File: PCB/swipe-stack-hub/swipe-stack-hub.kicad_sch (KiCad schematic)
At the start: 10 parts, among them J1 Barrel_Jack_Switch, U1 STM32F091RCTx, U2 LMR51430 (LMR54410), U3 CC2640R2FRGZR

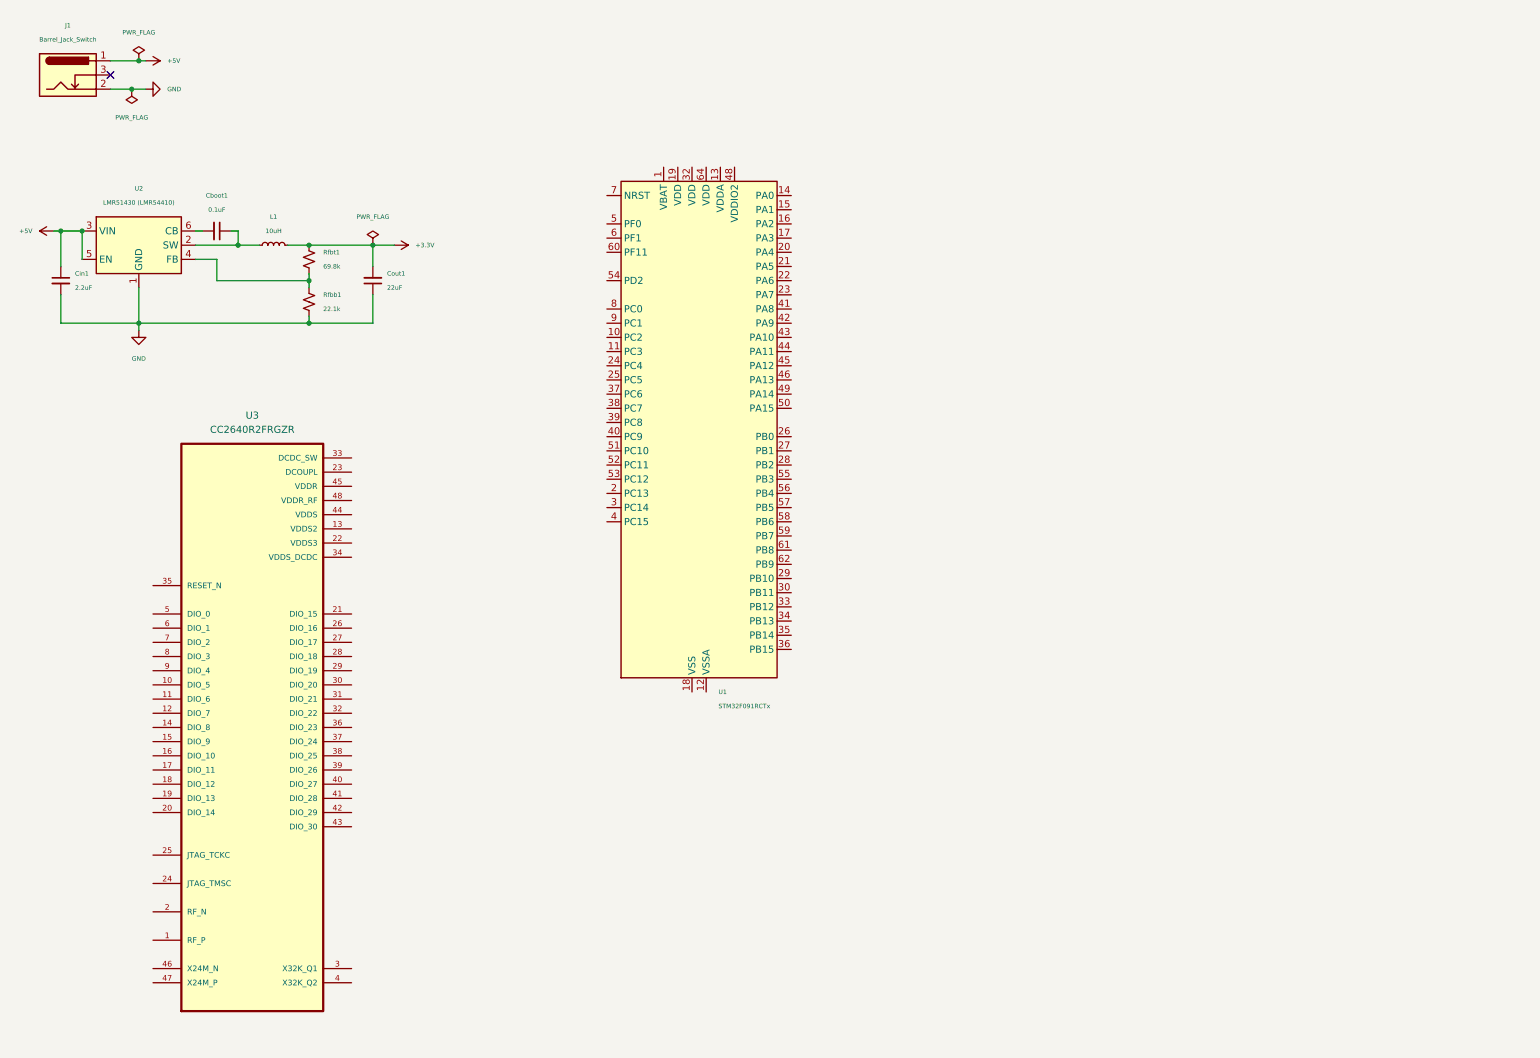
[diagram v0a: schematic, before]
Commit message: Updated swipe-stack hub schematic with HM19 modules as well as reset button circuitry for MCU
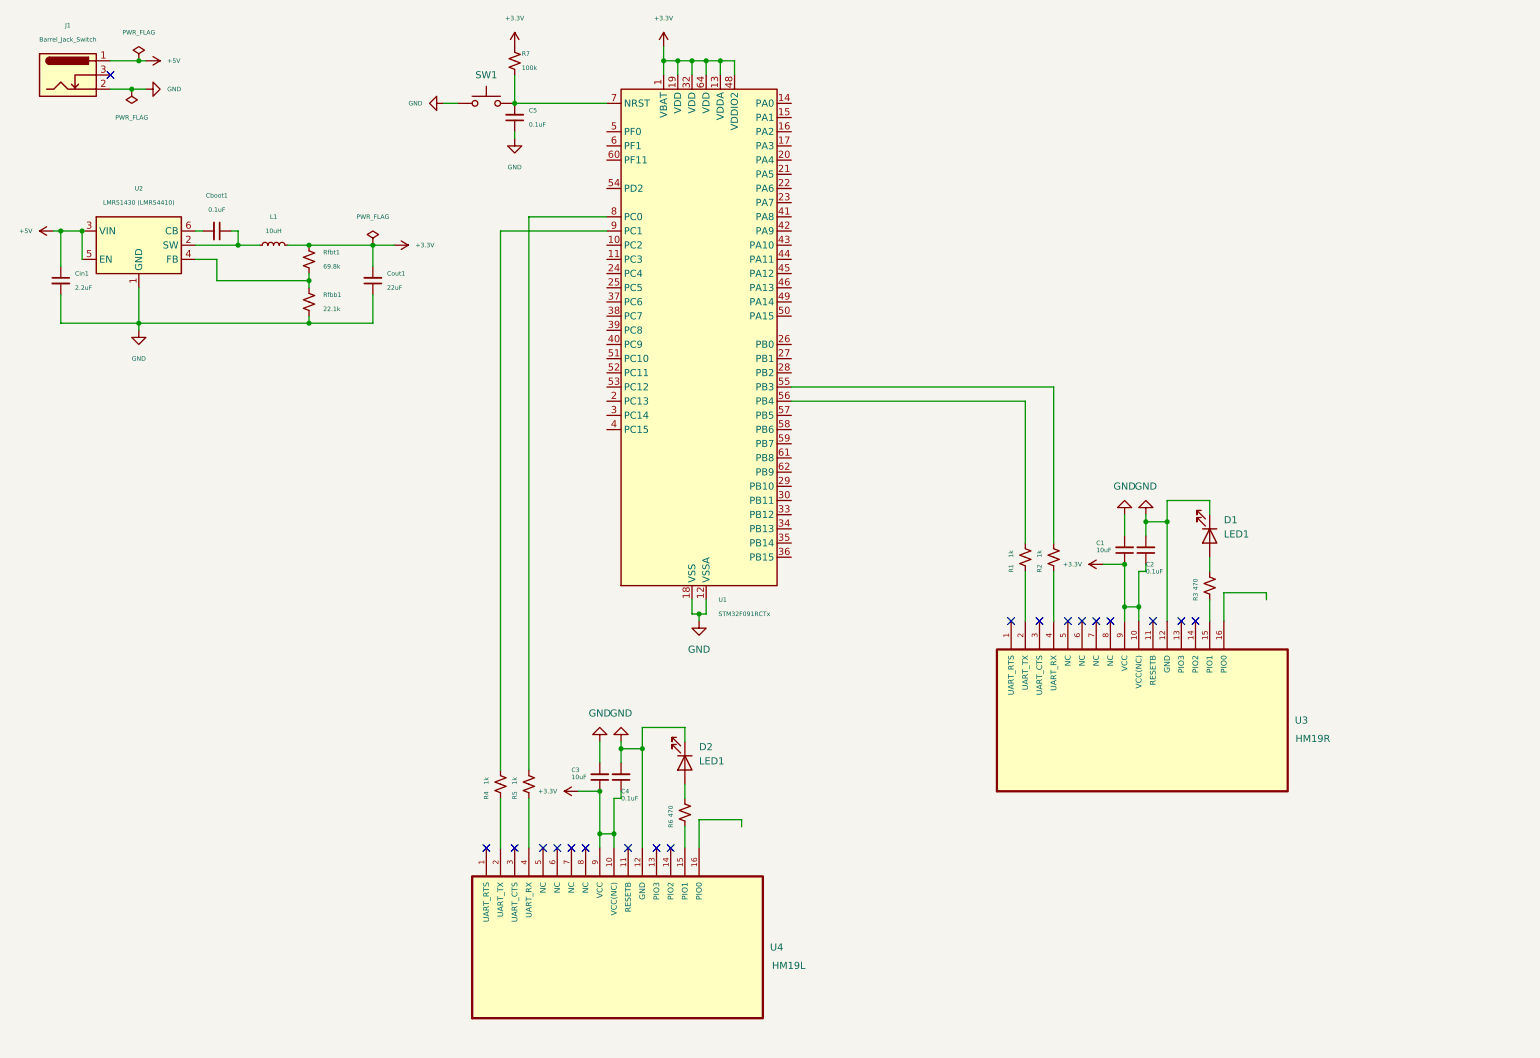
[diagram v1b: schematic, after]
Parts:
- removed U3: CC2640R2FRGZR, cc:QFN50P700X700X100-49N, symbol CC2640R2FRGZR:CC2640R2FRGZR
- added C1, C3: 10uF, symbol Device:C_Small
- added C2, C4, C5: 0.1uF, symbol Device:C_Small
- added D1, D2: LED1, symbol Device:LED
- added R1, R2, R4, R5: 1k, symbol Device:R_Small_US
- added R3, R6: 470, symbol Device:R_Small_US
- added R7: 100k, symbol Device:R_Small_US
- added SW1: ~, symbol Switch:SW_Push
- added U3: HM19R, hm:HM-11-MODULE, symbol HM11-19:CC2640R2FRGZR
- added U4: HM19L, hm:HM-11-MODULE, symbol HM11-19:CC2640R2FRGZR
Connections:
- net +3.3V: now also U1.1 (VBAT), U1.13 (VDDA), U1.19 (VDD), U1.32 (VDD), U1.48 (VDDIO2), U1.64 (VDD), C1.1, C2.1, C3.1, C4.1, R7.1, U3.10 (VCC(NC)), U3.9 (VCC), U4.10 (VCC(NC)), U4.9 (VCC)
- net GND: now also U1.12 (VSSA), U1.18 (VSS), U1.31 (VSS), U1.47 (VSS), U1.63 (VSS), C1.2, C2.2, C3.2, C4.2, C5.1, D1.1 (K), D2.1 (K), SW1.1, U3.12 (GND), U4.12 (GND)
- net at U1.55 (PB3): now also R2.2
- net at U1.56 (PB4): now also R1.2
- net at U1.7 (NRST): now also C5.2, R7.2, SW1.2
- net at U1.8 (PC0): now also R5.2
- net at U1.9 (PC1): now also R4.2
- new net: R3.1, U3.15 (PIO1)
- new net: D1.2 (A), R3.2
- new net: R1.1, U3.2 (UART_TX)
- new net: R4.1, U4.2 (UART_TX)
- new net: R5.1, U4.4 (UART_RX)
- new net: R6.1, U4.15 (PIO1)
- new net: D2.2 (A), R6.2
- new net: R2.1, U3.4 (UART_RX)
- no-connect marks 1 -> 19
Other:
- moved on the sheet: U1

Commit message: First cut of hub PCB
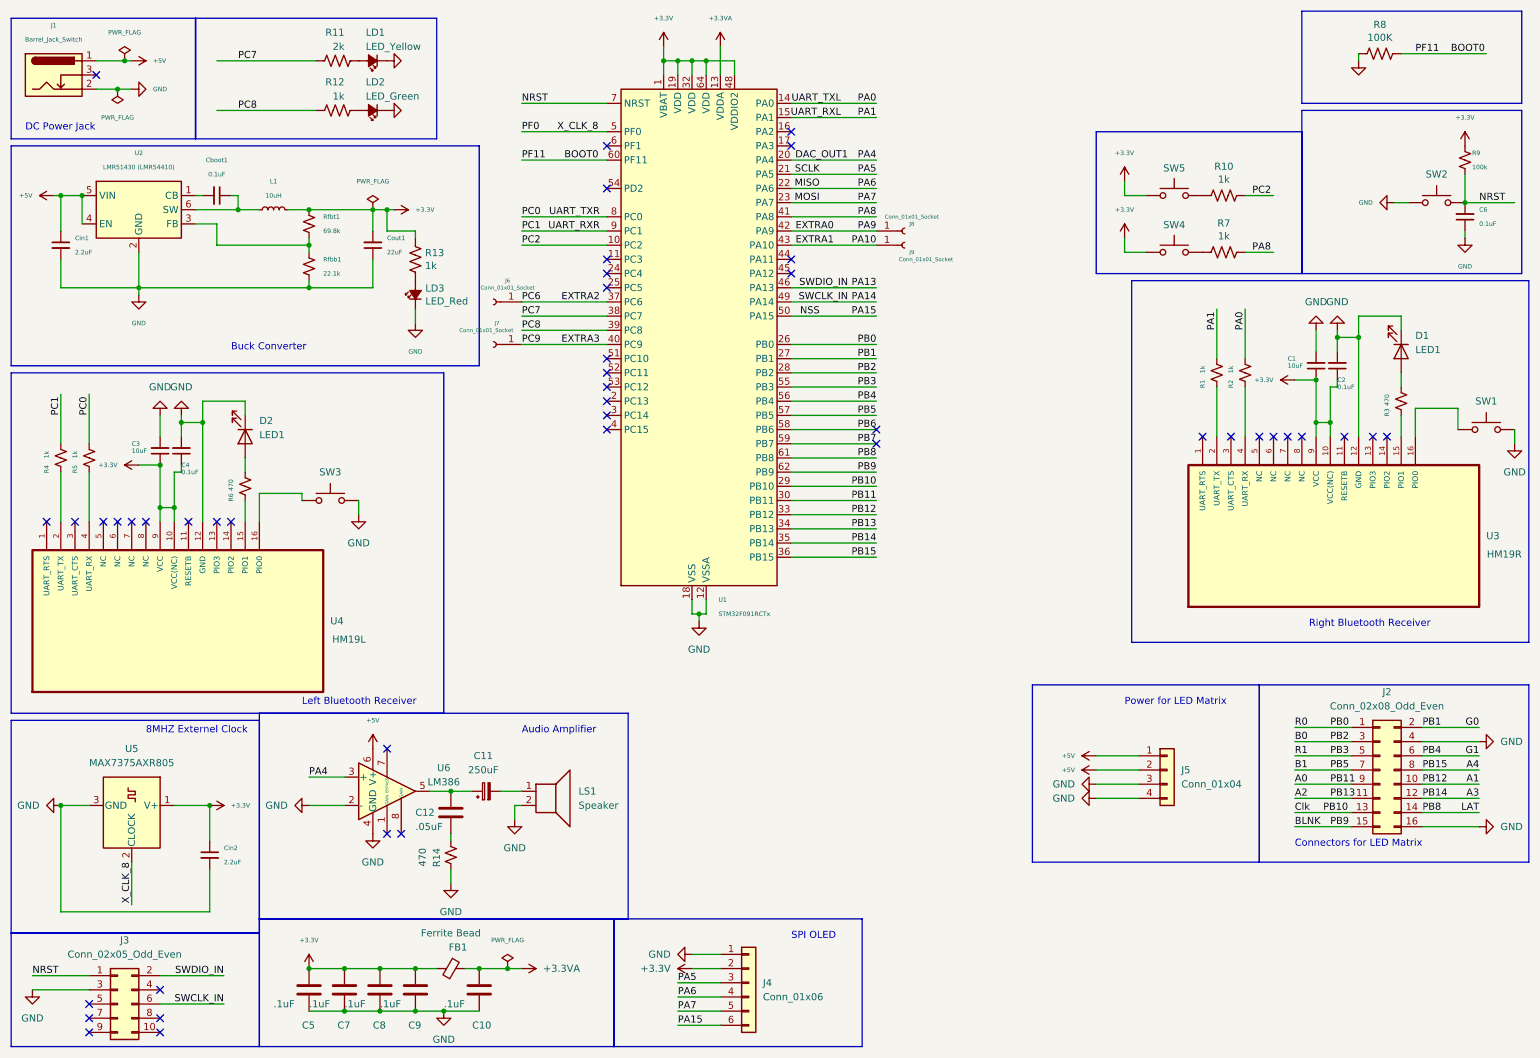
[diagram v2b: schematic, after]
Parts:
- removed C5: 0.1uF, symbol Device:C_Small
- removed R7: 100k, symbol Device:R_Small_US
- added C10, C5, C7, C8, C9: .1uF, Capacitor_SMD:C_0805_2012Metric_Pad1.18x1.45mm_HandSolder, symbol Device:C
- added C11: 250uF, Capacitor_SMD:C_0805_2012Metric_Pad1.18x1.45mm_HandSolder, symbol Device:C_Polarized_Small
- added C12: .05uF, Capacitor_SMD:C_0805_2012Metric_Pad1.18x1.45mm_HandSolder, symbol Device:C
- added C6: 0.1uF, Capacitor_SMD:C_0805_2012Metric_Pad1.18x1.45mm_HandSolder, symbol Device:C_Small
- added Cin2: 2.2uF, Capacitor_SMD:C_0805_2012Metric_Pad1.18x1.45mm_HandSolder, symbol Device:C_Small
- added FB1: Ferrite Bead, Inductor_SMD:L_0805_2012Metric_Pad1.15x1.40mm_HandSolder, symbol stm32f091-rescue:Ferrite_Bead_Small-Device
- added J2: Conn_02x08_Odd_Even, Connector_IDC:IDC-Header_2x08_P2.54mm_Vertical_SMD, symbol Connector_Generic:Conn_02x08_Odd_Even
- added J3: Conn_02x05_Odd_Even, Connector_IDC:IDC-Header_2x05_P2.54mm_Vertical_SMD, symbol Connector_Generic:Conn_02x05_Odd_Even
- added J4: Conn_01x06, Connector_JST:JST_EH_B6B-EH-A_1x06_P2.50mm_Vertical, symbol Connector_Generic:Conn_01x06
- added J5: Conn_01x04, Connector_JST:JST_EH_B4B-EH-A_1x04_P2.50mm_Vertical, symbol Connector_Generic:Conn_01x04
- added J6, J7, J8, J9: Conn_01x01_Socket, Connector_PinSocket_2.54mm:PinSocket_1x01_P2.54mm_Vertical, symbol Connector:Conn_01x01_Socket
- added LD1: LED_Yellow, LED_SMD:LED_0805_2012Metric_Pad1.15x1.40mm_HandSolder, symbol stm32f091-rescue:LED_Small_ALT-Device
- added LD2: LED_Green, LED_SMD:LED_0805_2012Metric_Pad1.15x1.40mm_HandSolder, symbol stm32f091-rescue:LED_Small_ALT-Device
- added LD3: LED_Red, LED_SMD:LED_0805_2012Metric_Pad1.15x1.40mm_HandSolder, symbol stm32f091-rescue:LED_Small_ALT-Device
- added LS1: Speaker, symbol Device:Speaker
- added R10, R12, R13, R7: 1k, Resistor_SMD:R_0805_2012Metric_Pad1.20x1.40mm_HandSolder, symbol Device:R_US
- added R11: 2k, Resistor_SMD:R_0805_2012Metric_Pad1.20x1.40mm_HandSolder, symbol Device:R_US
- added R14: 470, Resistor_SMD:R_0805_2012Metric_Pad1.20x1.40mm_HandSolder, symbol Device:R_Small_US
- added R8: 100K, Resistor_SMD:R_0805_2012Metric_Pad1.20x1.40mm_HandSolder, symbol Device:R_US
- added R9: 100k, Resistor_SMD:R_0805_2012Metric_Pad1.20x1.40mm_HandSolder, symbol Device:R_Small_US
- added SW2, SW3: ~, Button_Switch_SMD:SW_SPST_PTS645, symbol Switch:SW_Push
- added SW4, SW5: SW_Push, Button_Switch_SMD:SW_SPST_PTS645, symbol Switch:SW_Push
- added U5: MAX7375AXR805, Package_TO_SOT_SMD:SOT-323_SC-70_Handsoldering, symbol Oscillator:MAX7375AXR805
- added U6: LM386, Package_SO:SOIC-8-1EP_3.9x4.9mm_P1.27mm_EP2.29x3mm, symbol Amplifier_Audio:LM386
- C1, C2, C3, C4, Cboot1, Cin1, Cout1: footprint (none) -> Capacitor_SMD:C_0805_2012Metric_Pad1.18x1.45mm_HandSolder
- D1, D2: footprint (none) -> LED_SMD:LED_0805_2012Metric_Pad1.15x1.40mm_HandSolder
- L1: footprint (none) -> Inductor_SMD:L_0805_2012Metric_Pad1.15x1.40mm_HandSolder
- R1, R2, R3, R4, R5, R6, Rfbb1, Rfbt1: footprint (none) -> Resistor_SMD:R_0805_2012Metric_Pad1.20x1.40mm_HandSolder
- SW1: footprint (none) -> Button_Switch_SMD:SW_SPST_PTS645
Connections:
- net +3.3V: now also C5.1, C7.1, C8.1, C9.1, Cin2.1, FB1.2, J4.2 (Pin_2), R13.1, R9.1, SW4.1, SW5.1, U5.1 (V+); no longer U1.13 (VDDA)
- net +5V: now also U2.4 (EN), J5.1 (Pin_1), J5.2 (Pin_2), U6.6 (V+); no longer U2.3 (VIN)
- net GND: now also SW1.2, U2.2 (GND), C10.2, C5.2, C6.1, C7.2, C8.2, C9.2, Cin2.2, J2.16 (Pin_16), J2.4 (Pin_4), J3.3 (Pin_3), J4.1 (Pin_1), J5.3 (Pin_3), J5.4 (Pin_4), LD1.1 (K), LD2.1 (K), LD3.1 (K), LS1.2, R14.1, R8.2, SW2.1, SW3.2, U5.3 (GND), U6.2 (-), U6.4 (GND); no longer SW1.1, U2.1 (GND)
- net at Rfbb1.1, Rfbt1.2: now also U2.3 (FB); no longer U2.4 (FB)
- net G1: now reaches U1.56 (PB4)
- net G1: now also J2.6 (Pin_6); no longer R1.2
- net at Cboot1.1, L1.1: now also U2.6 (SW); no longer U2.2 (SW)
- net PC1: now reaches R4.2, U1.9 (PC1)
- net NRST: now reaches U1.7 (NRST)
- net NRST: now also C6.2, J3.1 (Pin_1), R9.2, SW2.2; no longer SW1.2
- net PC0: now reaches R5.2, U1.8 (PC0)
- net at Cboot1.2: now also U2.1 (CB); no longer U2.6 (CB)
- net PA0: now reaches R2.2
- net PA0: now also U1.14 (PA0); no longer U1.55 (PB3)
- net at U3.16 (PIO0): now also SW1.1
- net at U4.16 (PIO0): now also SW3.1
- net PC2: now reaches U1.10 (PC2)
- net PC2: now also R10.1
- net PA1: now reaches U1.15 (PA1)
- net PA1: now also R1.2
- net DAC_OUT1: now reaches U1.20 (PA4)
- net DAC_OUT1: now also U6.3 (+)
- net PA5: now reaches U1.21 (PA5)
- net PA5: now also J4.3 (Pin_3)
- net MISO: now reaches U1.22 (PA6)
- net MISO: now also J4.4 (Pin_4)
- net MOSI: now reaches U1.23 (PA7)
- net MOSI: now also J4.5 (Pin_5)
- net PB0: now reaches U1.26 (PB0)
- net PB0: now also J2.1 (Pin_1)
- net G0: now reaches U1.27 (PB1)
- net G0: now also J2.2 (Pin_2)
- net B0: now reaches U1.28 (PB2)
- net B0: now also J2.3 (Pin_3)
- net Clk: now reaches U1.29 (PB10)
- net Clk: now also J2.13 (Pin_13)
- net A0: now reaches U1.30 (PB11)
- net A0: now also J2.9 (Pin_9)
- net A1: now reaches U1.33 (PB12)
- net A1: now also J2.10 (Pin_10)
- net A2: now reaches U1.34 (PB13)
- net A2: now also J2.11 (Pin_11)
- net A3: now reaches U1.35 (PB14)
- net A3: now also J2.12 (Pin_12)
- net A4: now reaches U1.36 (PB15)
- net A4: now also J2.8 (Pin_8)
- net EXTRA2: now reaches U1.37 (PC6)
- net EXTRA2: now also J6.1 (Pin_1)
- net PC7: now reaches U1.38 (PC7)
- net PC7: now also R11.2
- net PC8: now reaches U1.39 (PC8)
- net PC8: now also R12.2
- net EXTRA3: now reaches U1.40 (PC9)
- net EXTRA3: now also J7.1 (Pin_1)
- net PA8: now reaches U1.41 (PA8)
- net PA8: now also R7.1
- net EXTRA0: now reaches U1.42 (PA9)
- net EXTRA0: now also J8.1 (Pin_1)
- net EXTRA1: now reaches U1.43 (PA10)
- net EXTRA1: now also J9.1 (Pin_1)
- net PA13: now reaches U1.46 (PA13)
- net PA13: now also J3.2 (Pin_2)
- net PA14: now reaches U1.49 (PA14)
- net PA14: now also J3.6 (Pin_6)
- net PF0: now reaches U1.5 (PF0)
- net PF0: now also U5.2 (CLOCK)
- net NSS: now reaches U1.50 (PA15)
- net NSS: now also J4.6 (Pin_6)
- net B1: now reaches U1.57 (PB5)
- net B1: now also J2.7 (Pin_7)
- net PB6: now reaches U1.58 (PB6)
- net PB7: now reaches U1.59 (PB7)
- net BOOT0: now reaches U1.60 (PF11)
- net BOOT0: now also R8.1
- net LAT: now reaches U1.61 (PB8)
- net LAT: now also J2.14 (Pin_14)
- net BLNK: now reaches U1.62 (PB9)
- net BLNK: now also J2.15 (Pin_15)
- new net: LD3.2 (A), R13.2
- new net: C11.1, C12.1, U6.5
- new net: C11.2, LS1.1
- new net: C12.2, R14.2
- new net: LD2.2 (A), R12.1
- new net: R10.2, SW5.2
- new net: LD1.2 (A), R11.1
- new net: R7.2, SW4.2
- new net +3.3VA: C10.1, FB1.1, U1.13 (VDDA)
- new net PB3: J2.5 (Pin_5), U1.55 (PB3)
- no-connect marks 19 -> 45
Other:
- note added: "8MHZ Externel Clock"
- note added: "Audio Amplifier"
- note added: "Buck Converter"
- note added: "Connectors for LED Matrix"
- note added: "DC Power Jack"
- note added: "Left Bluetooth Receiver"
- note added: "Power for LED Matrix"
- note added: "Right Bluetooth Receiver"
- note added: "SPI OLED"
- moved on the sheet: C1, C2, C3, C4, Cboot1, Cin1, Cout1, D1, D2, J1, L1, R1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

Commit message: Justin's version of hub PCB
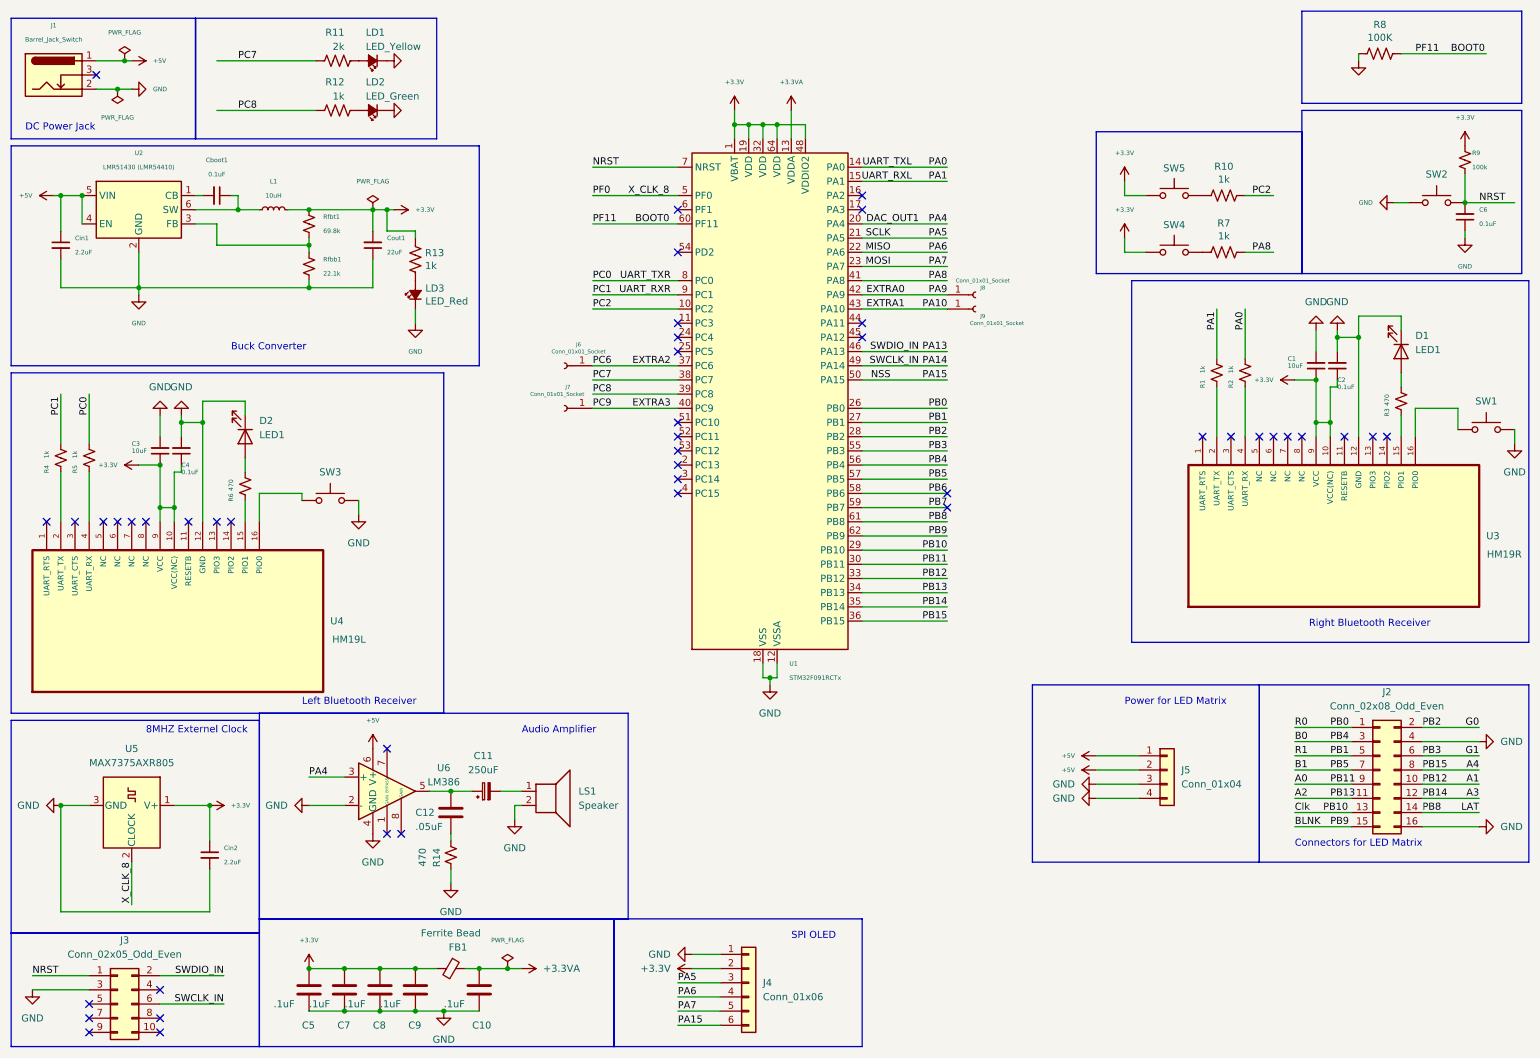
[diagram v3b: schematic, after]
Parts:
- LS1: footprint (none) -> 477:Speaker
- U3, U4: footprint hm:HM-11-MODULE -> 477:HM-11-MODULE
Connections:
- net B0: now also U1.56 (PB4); no longer U1.28 (PB2)
- net G0: now also U1.28 (PB2); no longer U1.27 (PB1)
- net G1: now also U1.55 (PB3); no longer U1.56 (PB4)
- net PB3 renamed PB1
- net PB1: now also U1.27 (PB1); no longer U1.55 (PB3)
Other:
- moved on the sheet: J6, J7, J8, J9, U1
